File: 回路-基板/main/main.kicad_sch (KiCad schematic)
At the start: 49 parts, among them J1 Conn_01x07_Pin, Q1 PMOS, Q2 NMOS, Q3 PMOS, Q4 NMOS, SW1 SW_SPDT, SW2 SW_Push, SW3 SW_Push, SW4 SW_Push, SW5 SW_Push, SW6 SW_Push, U1 TWE-L-WX, U2 LM1117MP-3.3

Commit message: 回路図/PCB両方一応完成した
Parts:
- removed Q1, Q3: PMOS, symbol Simulation_SPICE:PMOS
- removed Q2, Q4: NMOS, symbol Simulation_SPICE:NMOS
- removed R1: 10k, Resistor_SMD:R_0805_2012Metric, symbol Device:R_Small
- removed R2, R3: 100k, Resistor_SMD:R_0805_2012Metric, symbol Device:R_Small
- removed SW1: SW_SPDT, @2024-cansat:SS12D01G4, symbol Switch:SW_SPDT
- added J2, J3, J4, J5: Conn_01x08_Pin, @2024-cansat:Pin-Extender, symbol Connector:Conn_01x08_Pin
- BT1, BT2, BT3: value 3V -> 1.5V; footprint @2024-cansat:BHSD-2032-SM -> @2024-cansat:AAA-holder
- J1: footprint Connector_PinHeader_2.54mm:PinHeader_1x07_P2.54mm_Horizontal -> Connector_PinSocket_2.54mm:PinSocket_1x07_P2.54mm_Vertical
- renumbered C3 to C2, C4 to C3, C5 to C4, C6 to C5, C7 to C6, C8 to C7, C9 to C8, C10 to C9, R4 to R1, R13 to R10, R14 to R11, R15 to R12, R16 to R13, R17 to R14, R5 to R2, R6 to R3, R7 to R4, R8 to R5, R9 to R6, R10 to R7, R11 to R8, R12 to R9, SW2 to SW1, SW3 to SW2, SW4 to SW3, SW5 to SW4, SW6 to SW5
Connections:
- net BTN-CENTER is gone; now on net 23: C5.2, R9.2, SW1.1
- net BTN-DOWN is gone; now on net 19: C8.2, R12.2, SW4.1
- net BTN-LEFT is gone; now on net 22: C7.2, R11.2, SW3.1
- net BTN-RIGHT is gone; now on net 24: C9.2, R13.2, SW5.1
- net BTN-UP is gone; now on net 25: C6.2, R10.2, SW2.1
- net +3.3V: now also JP1.1 (A), J2.5 (Pin_5); no longer J1.6 (Pin_6)
- net 1: now also J2.1 (Pin_1)
- net 10: now also J3.2 (Pin_2)
- net 11: now also J3.3 (Pin_3)
- net 12: now also J3.4 (Pin_4)
- net 13: now also J3.5 (Pin_5); no longer JP1.1 (A)
- net 14: now also J3.6 (Pin_6)
- net 15: now also J3.7 (Pin_7)
- net 16: now also J3.8 (Pin_8)
- net 17: now also J4.1 (Pin_1)
- net 18: now also J4.2 (Pin_2)
- net 19: now also J4.3 (Pin_3)
- net 2: now also J2.2 (Pin_2)
- net 21: now also J4.5 (Pin_5)
- net 22: now also J4.6 (Pin_6)
- net 23: now also J4.7 (Pin_7)
- net 24: now also J4.8 (Pin_8)
- net 25: now also J5.1 (Pin_1)
- net 26: now also J5.2 (Pin_2)
- net 27: now also J5.3 (Pin_3)
- net 3: now also J2.3 (Pin_3)
- net 4: now also J2.4 (Pin_4)
- net 6: now also J2.6 (Pin_6)
- net 7: now also J2.7 (Pin_7)
- net 8: now also J2.8 (Pin_8)
- net 9: now also J3.1 (Pin_1)
- net GND: now also J4.4 (Pin_4), J5.4 (Pin_4), J5.6 (Pin_6), J5.7 (Pin_7), J5.8 (Pin_8)
- net at JP1.2 (B): now also J1.6 (Pin_6); no longer J1.7 (Pin_7)
- no-connect marks 3 -> 5
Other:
- note added: "PIN"
- note removed: "UART-SWITCHING"
- note removed: "考え中..."

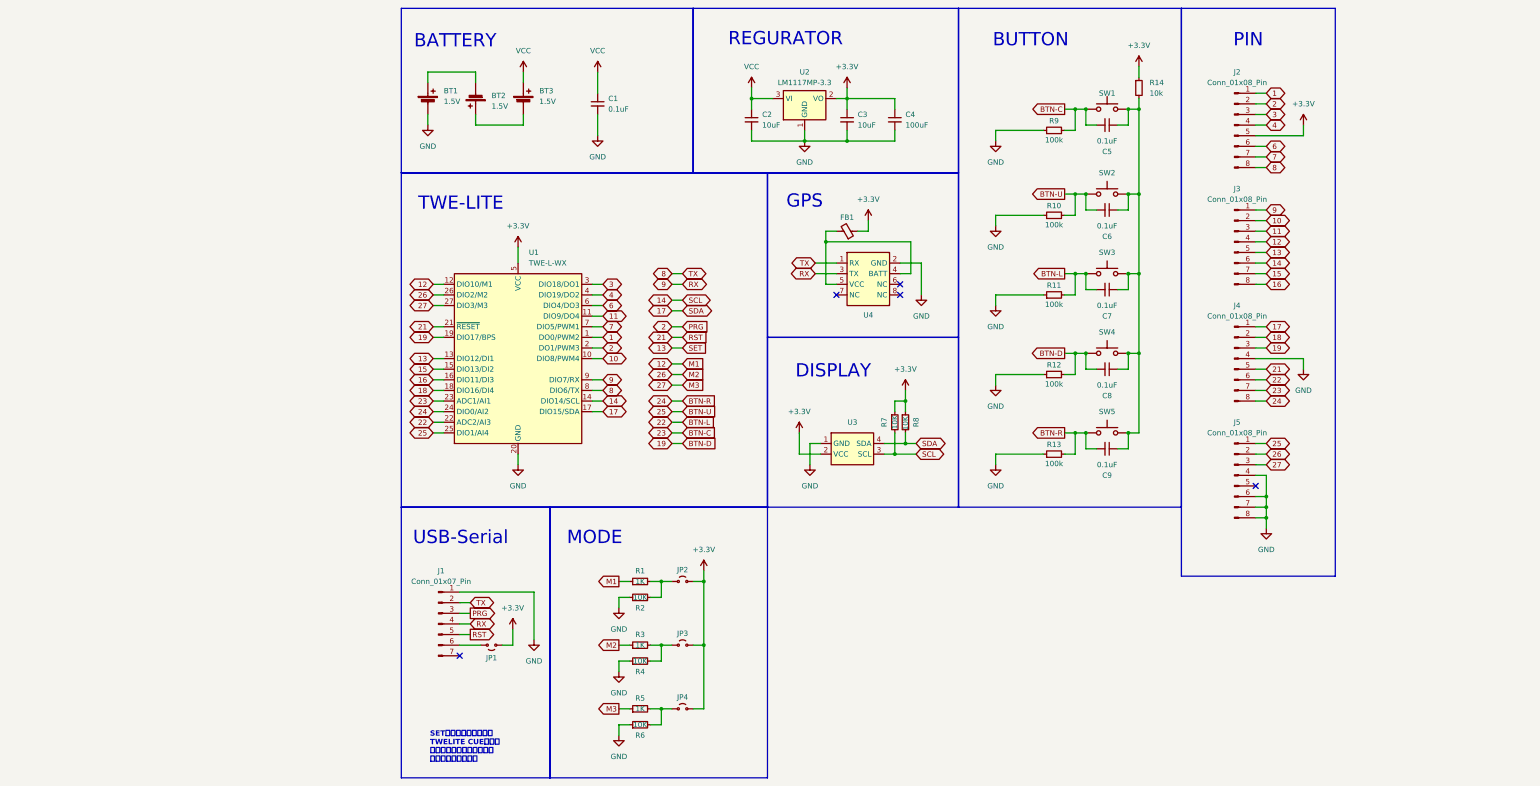
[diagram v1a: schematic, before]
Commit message: メインのPCBを更新した
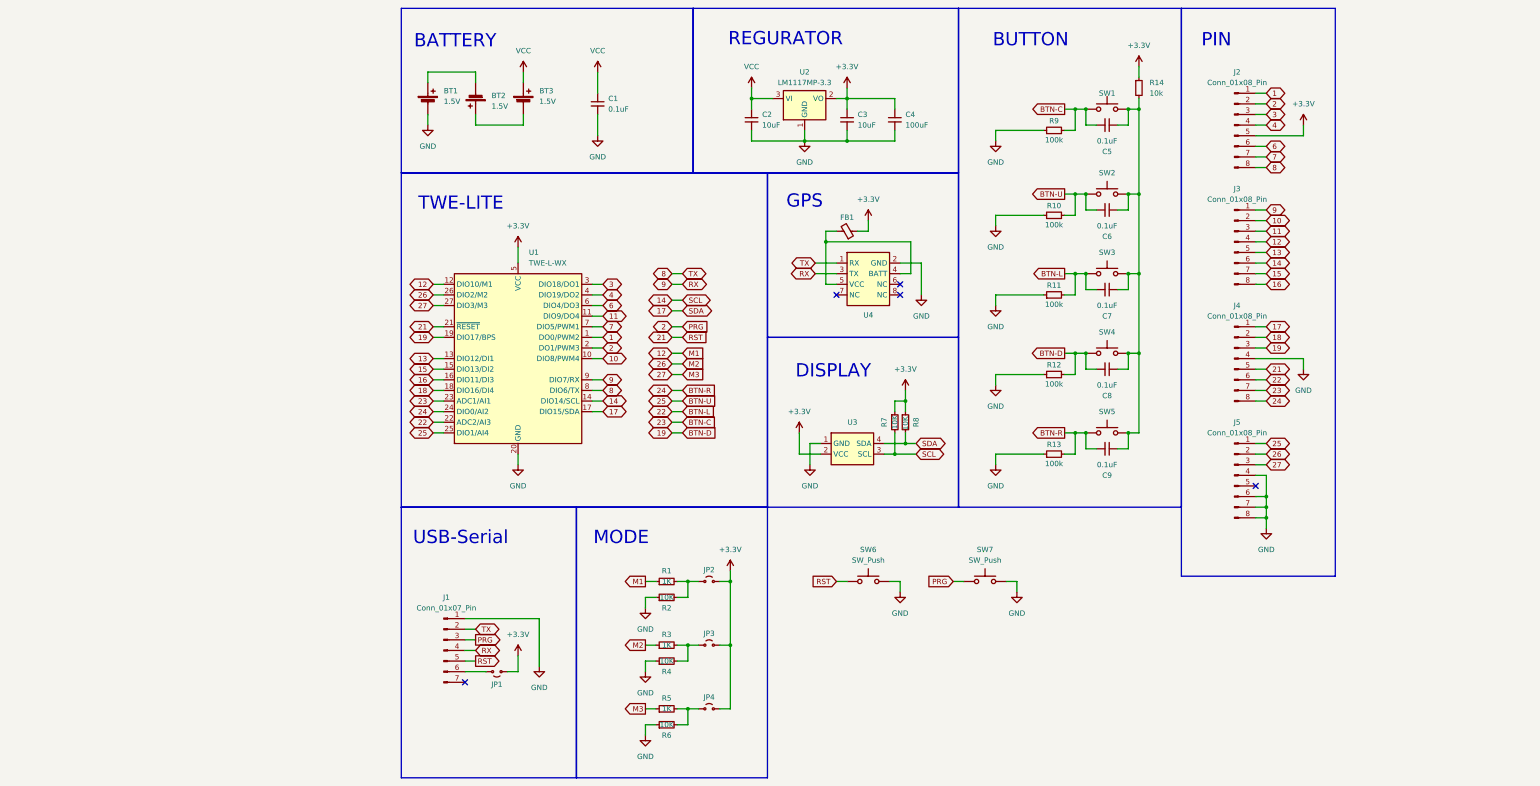
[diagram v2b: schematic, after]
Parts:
- added SW6, SW7: SW_Push, @2024-cansat:Tactile1, symbol Switch:SW_Push
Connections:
- net 2: now also SW7.1
- net 21: now also SW6.1
- net GND: now also SW6.2, SW7.2
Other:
- note removed: "SETピンは拡張制御信号 TWELITE CUEなどで インタラクティブモードに 移行するために使用"
- moved on the sheet: J1, JP1, JP2, JP3, JP4, R1, R2, R3, R4, R5, R6

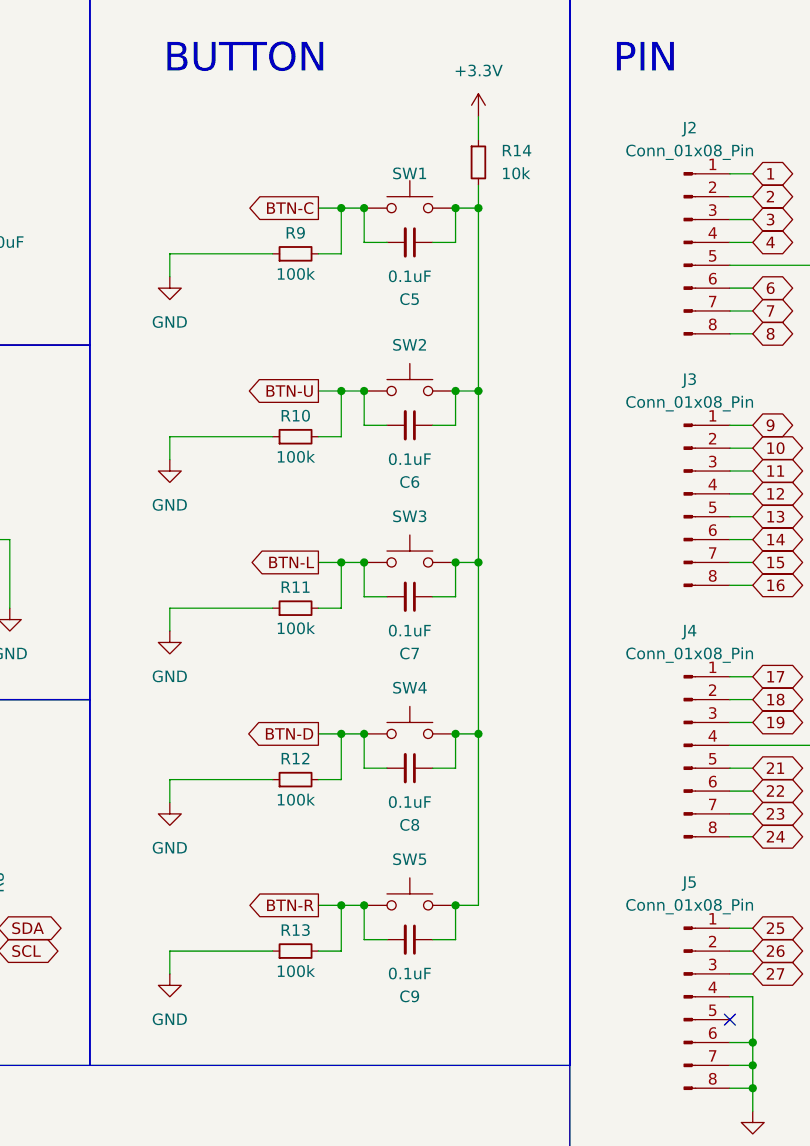
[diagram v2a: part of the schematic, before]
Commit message: JLCPCB用の出力ファイルなどを追加
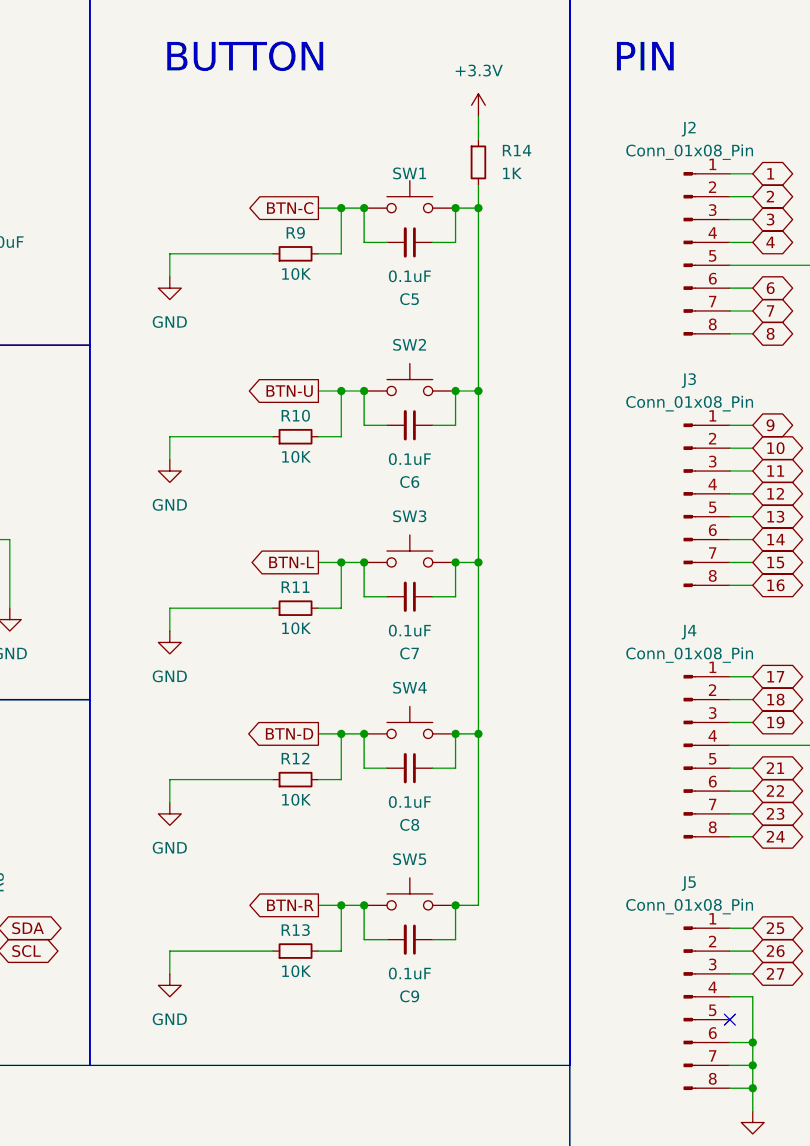
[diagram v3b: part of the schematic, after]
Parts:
- R10, R11, R12, R13, R9: value 100k -> 10K
- R14: value 10k -> 1K
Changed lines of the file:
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@@
 			)
 		)
-		(property "Value" "100k"
+		(property "Value" "10K"
 			(at 168.91 102.616 90)
 			(effects
@@
 			)
 		)
-		(property "Value" "100k"
+		(property "Value" "10K"
 			(at 168.91 121.666 90)
 			(effects
@@
 			)
 		)
-		(property "Value" "100k"
+		(property "Value" "10K"
 			(at 168.91 44.196 90)
 			(effects
@@
 			)
 		)
-		(property "Value" "100k"
+		(property "Value" "10K"
 			(at 168.91 64.516 90)
 			(effects
@@
 			)
 		)
-		(property "Value" "100k"
+		(property "Value" "10K"
 			(at 168.91 83.566 90)
 			(effects
@@
 			)
 		)
-		(property "Value" "10k"
+		(property "Value" "1K"
 			(at 191.77 33.02 0)
 			(effects

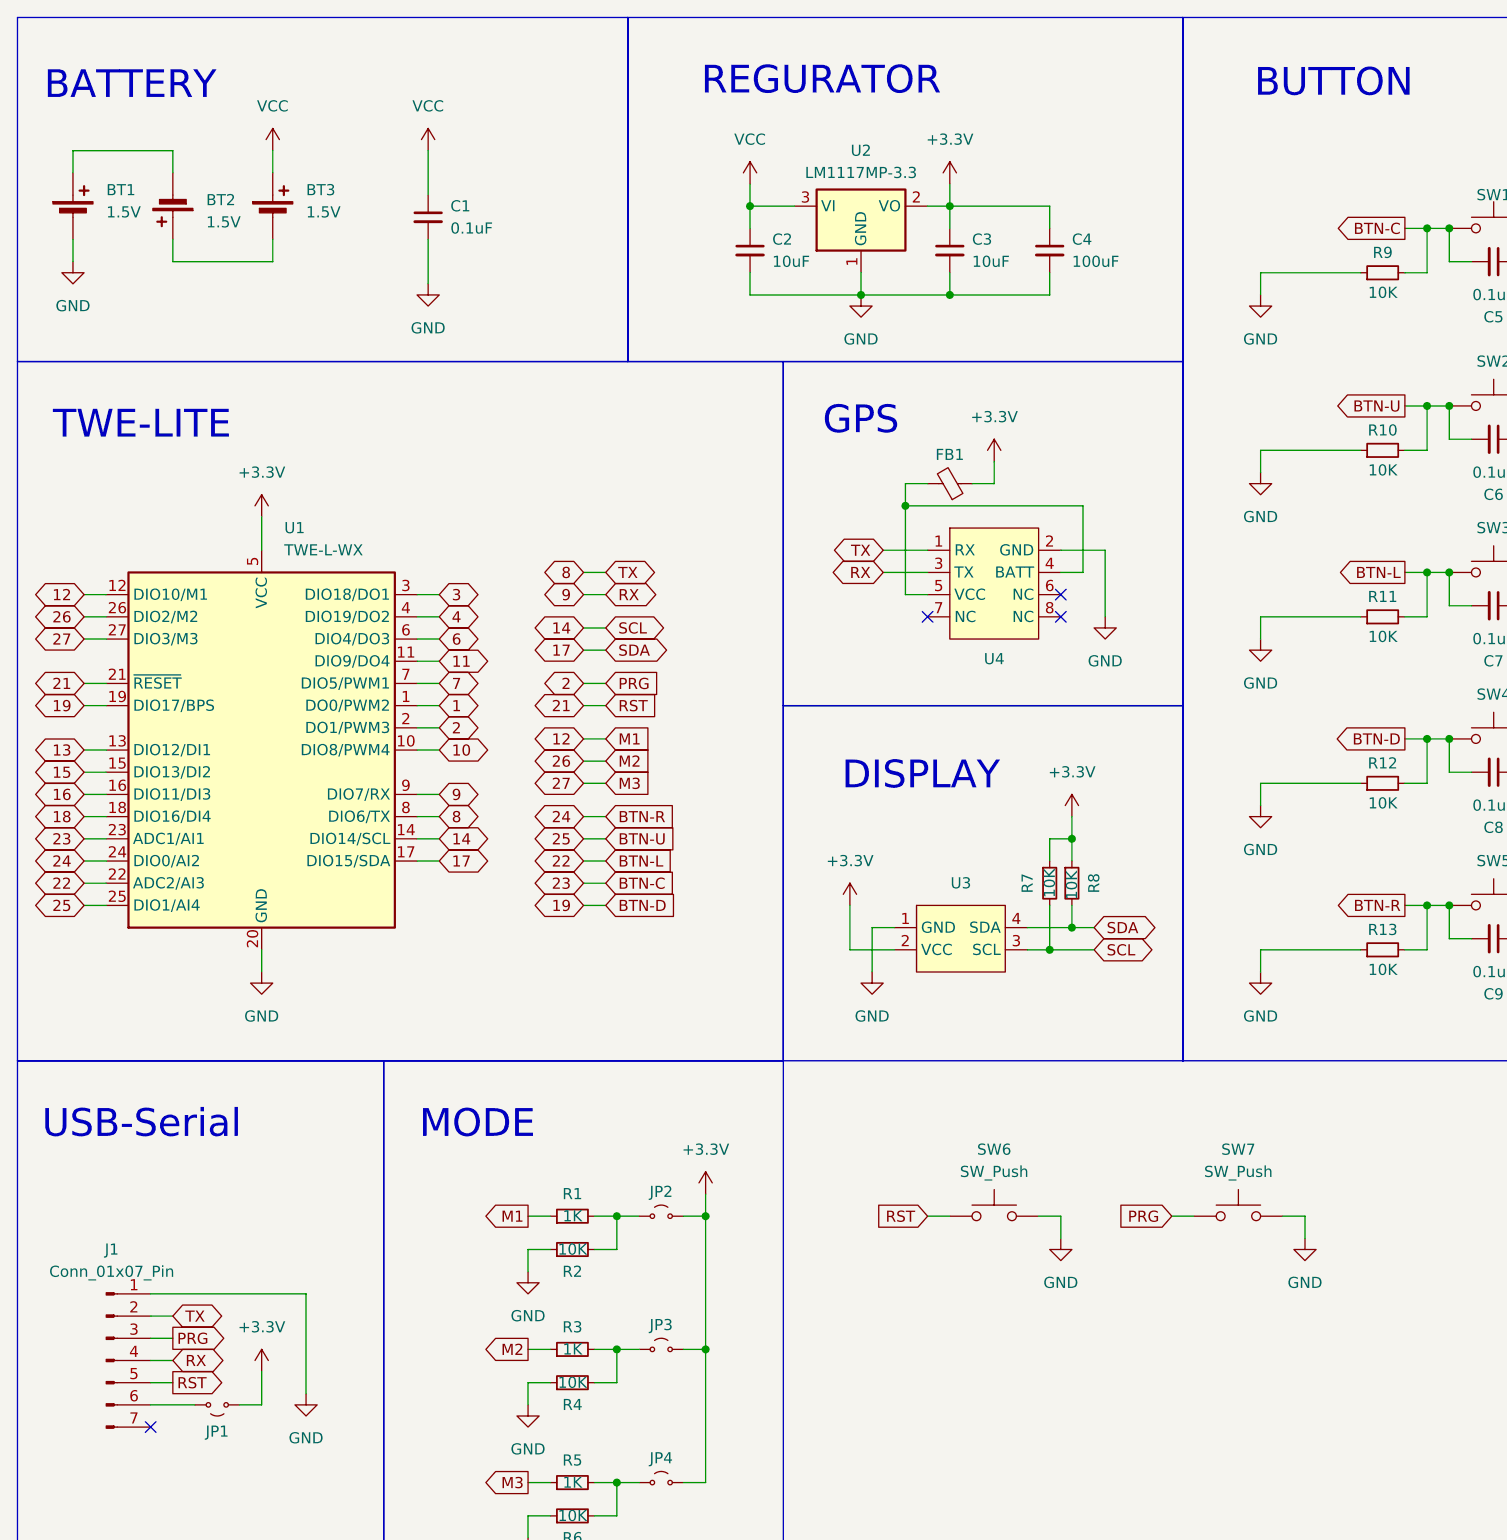
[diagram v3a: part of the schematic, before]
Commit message: 電源用のLEDのつけ忘れを慌てて修正したよ
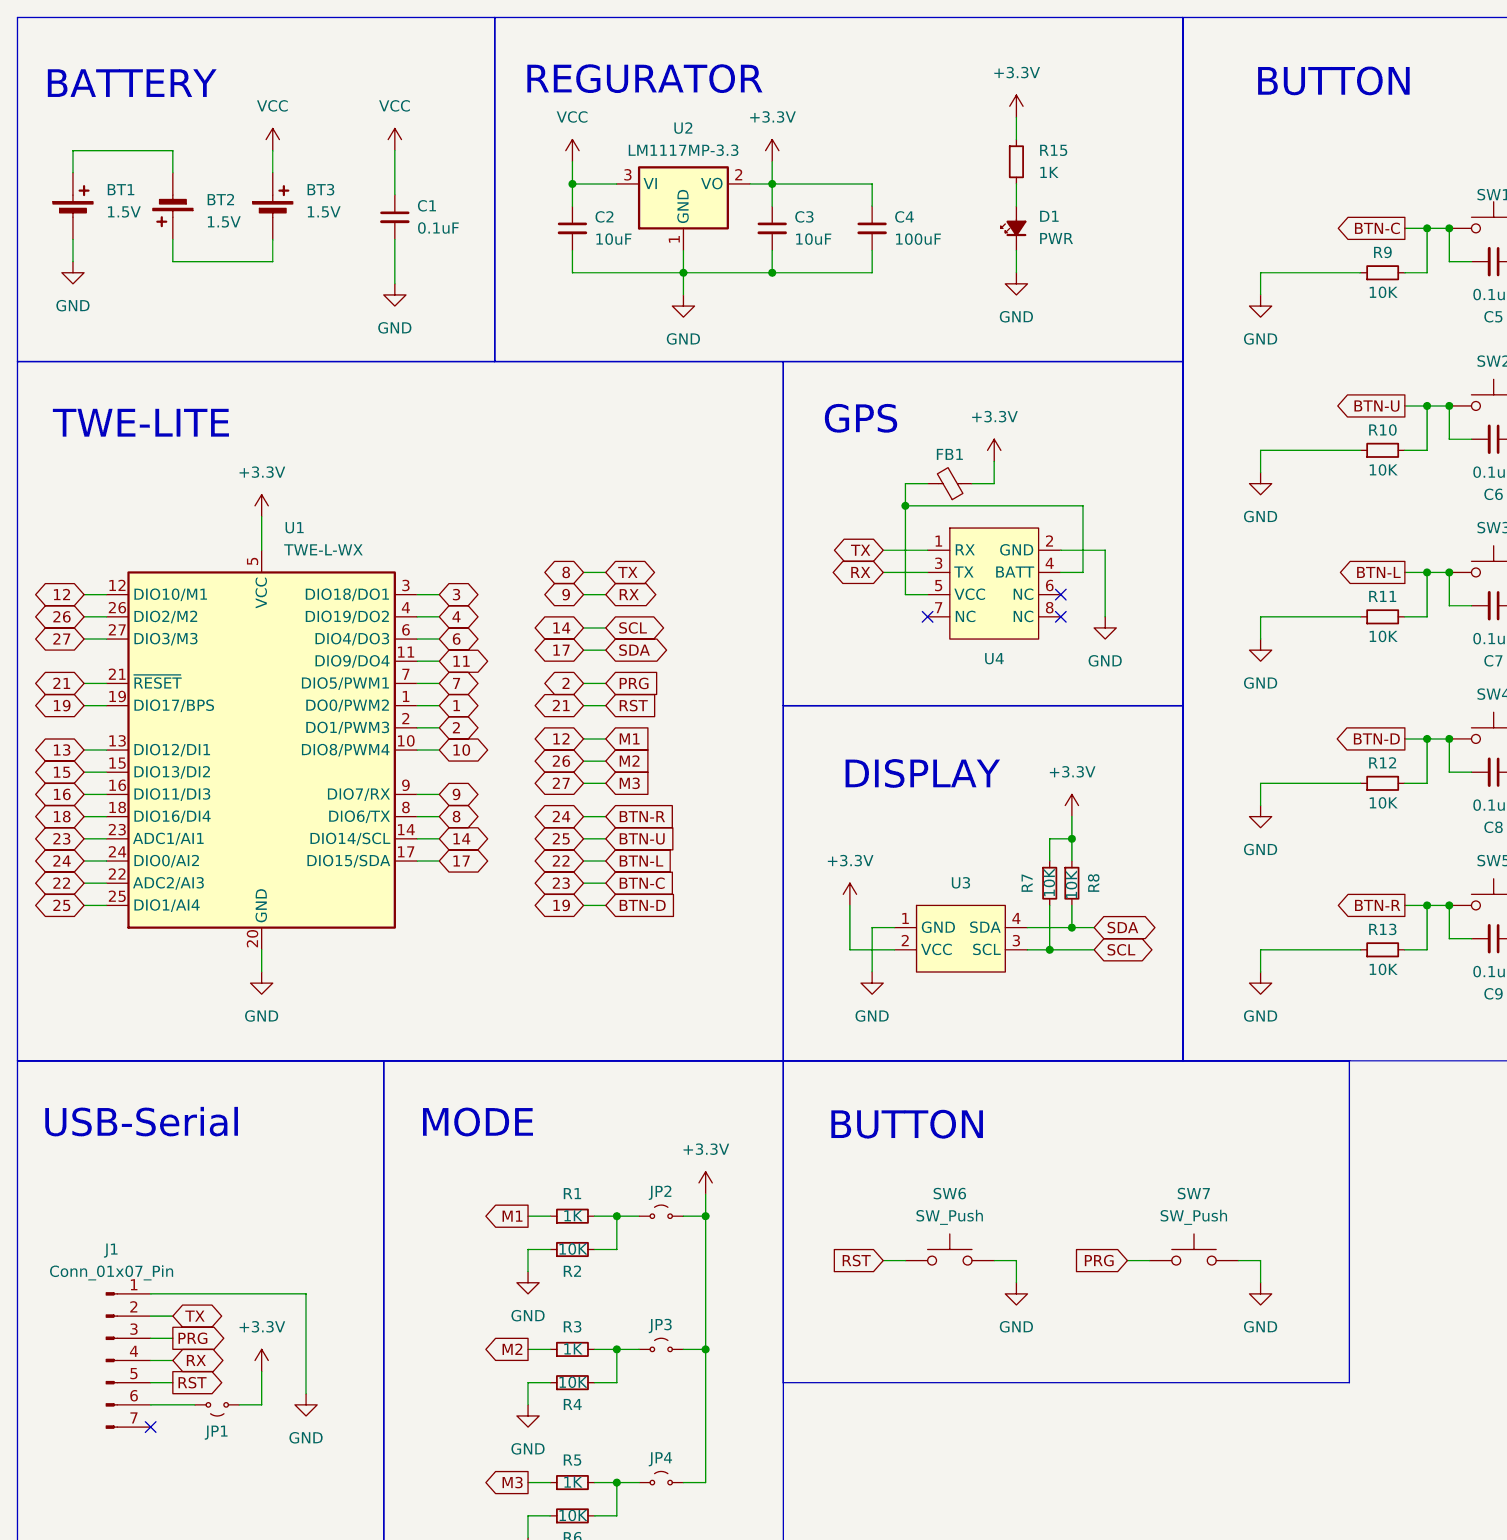
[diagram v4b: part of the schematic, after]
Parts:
- added D1: PWR, LED_SMD:LED_0805_2012Metric, symbol Device:LED_Small_Filled
- added R15: 1K, Resistor_SMD:R_0805_2012Metric, symbol Device:R_Small
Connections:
- net +3.3V: now also R15.1
- net GND: now also D1.1 (K)
- new net: D1.2 (A), R15.2
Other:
- moved on the sheet: C1, C2, C3, C4, SW6, SW7, U2
